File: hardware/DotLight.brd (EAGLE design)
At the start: 25.4 x 43.5 mm, 21 parts, among them Q1 BSH103, Q2 BSH103

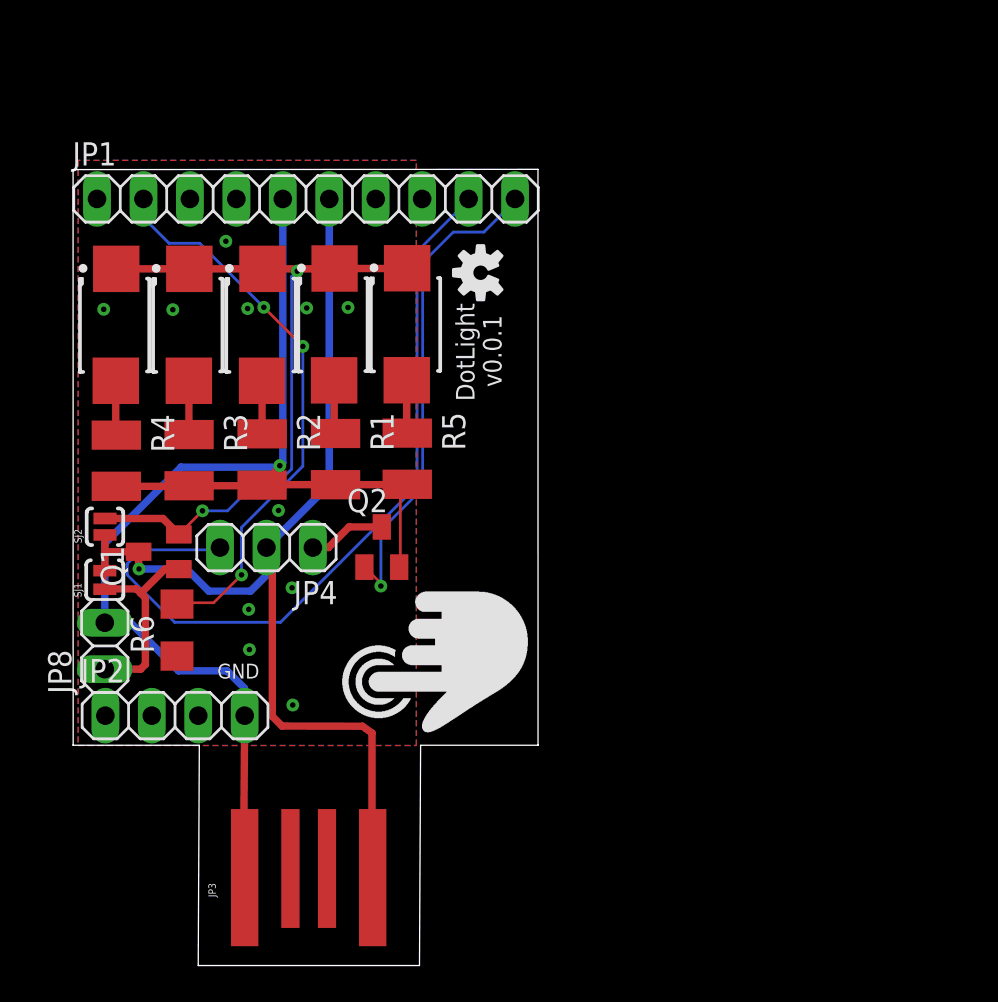
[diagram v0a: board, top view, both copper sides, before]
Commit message: Mirror parts for space for PIR
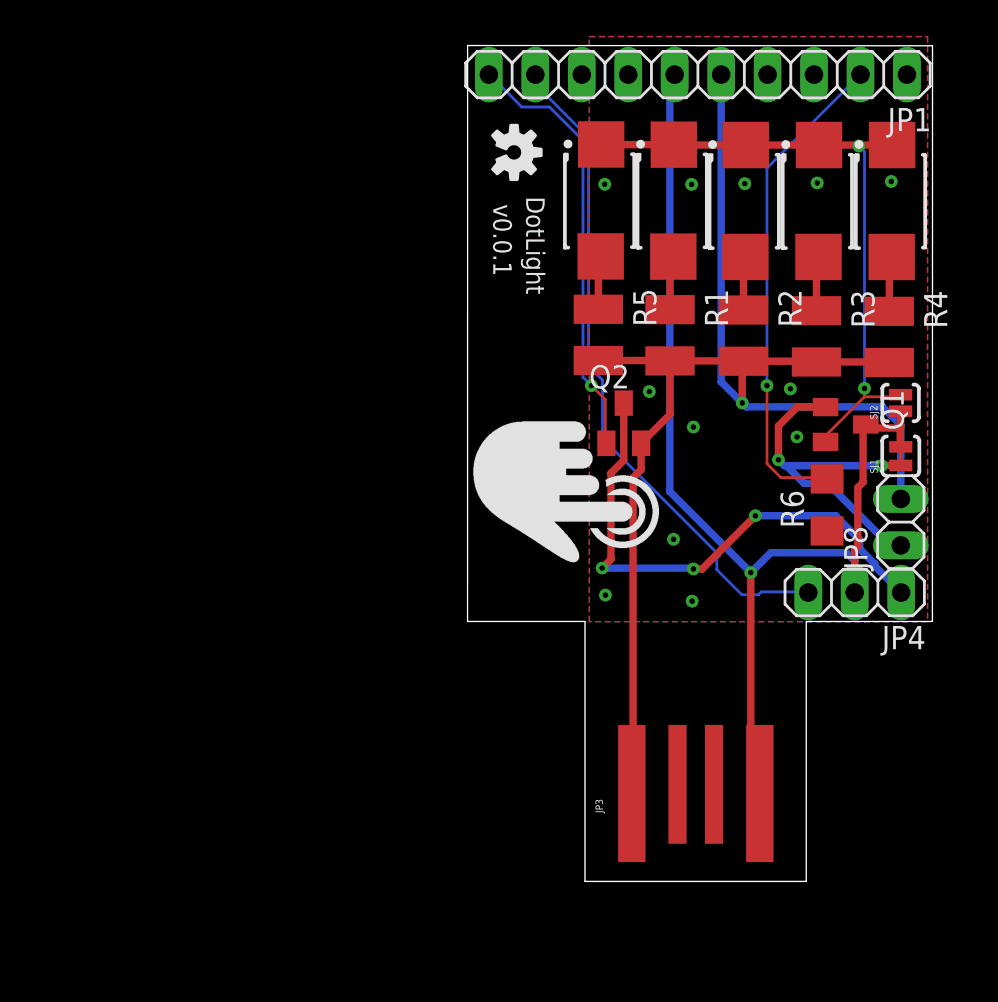
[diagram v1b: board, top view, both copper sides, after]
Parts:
- removed JP2: (no value), pinhead:1X04
- moved JP8 44.1 mm to (45.4, 23.3)
- moved SJ1 44.1 mm to (45.4, 26.9)
- moved SJ2 44.0 mm to (45.4, 29.8)
- moved LED3 43.0 mm to (44.9, 40.9)
- moved R4 42.8 mm to (44.8, 33.5)
- moved Q1 38.2 mm to (42.4, 28.7), turned to 270 degrees
- moved R6 36.2 mm to (41.4, 24.3)
- moved LED2 35.1 mm to (40.9, 40.9)
- moved R3 35.0 mm to (40.8, 33.5)
- moved JP4 32.3 mm to (42.9, 19.5)
- moved LED1 27.3 mm to (36.9, 40.9)
- moved R2 27.2 mm to (36.8, 33.5)
- moved JP1 22.5 mm to (34.3, 47.8), turned to 180 degrees
- moved JP3 21.7 mm to (34.2, 8.68)
- moved LED4 19.7 mm to (32.9, 40.9)
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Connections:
- removed net +3V3: JP2.3
- removed net SCL: JP2.2
- removed net SDA: JP2.1
- net GND: no longer JP2.4
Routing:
- net N$3: track 4.24 -> 29.2 mm, vias 0 -> 3
- net LEDS: track 11.0 -> 19.8 mm, vias 0 -> 2
- net MISO: track 42.9 -> 36.9 mm
- net VIN_PIN: track 57.7 -> 62.9 mm
- net N$4: track 40.3 -> 35.2 mm
- net ADC: track 30.7 -> 27.0 mm, vias 3 -> 1
- net MOSI: track 26.6 -> 23.7 mm
- net GND: track 72.1 -> 74.5 mm
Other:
- board size 25.4 x 43.5 mm -> 25.4 x 45.7 mm
- board text added: "LEDS ENABLE"
- board text added: "PIR"
- board text removed: "GND"

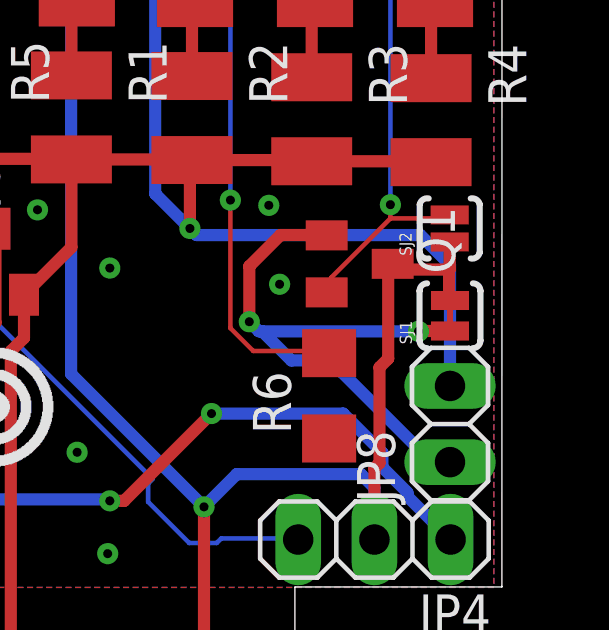
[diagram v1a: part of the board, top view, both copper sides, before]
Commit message: Mirror parts for space for PIR
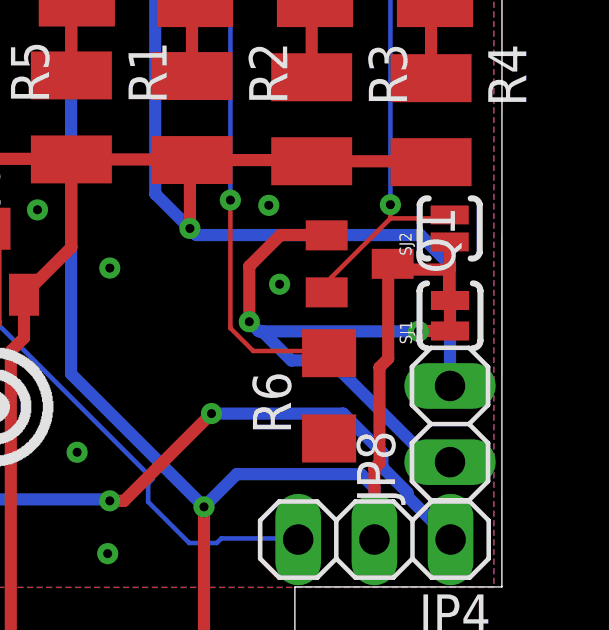
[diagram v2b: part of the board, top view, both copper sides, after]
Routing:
- net N$1: track 0.00 -> 0.73 mm
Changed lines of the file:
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@@
 <via x="43.1292" y="43.8912" extent="1-16" drill="0.3"/>
+</signal>
+<signal name="N$1">
+<wire x1="45.42" y1="27.32" x2="45.42" y2="26.59" width="0.4064" layer="1"/>
 </signal>
 </signals>

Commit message: Adjust solderjumpers
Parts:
- removed SJ1: SOLDERJUMPERTRACE, SparkFun-Retired:SJ_2S-TRACE
- moved JP1 21.2 mm to (13.4, 44.6)
- moved JP3 21.2 mm to (13.3, 5.47)
- moved JP8 21.2 mm to (24.5, 20.1)
- moved LED4 21.2 mm to (12.0, 37.7)
- moved LED5 21.2 mm to (8.04, 37.7)
- moved Q2 21.2 mm to (9.35, 25.5)
- moved R2 21.2 mm to (15.9, 30.3)
- moved R3 21.2 mm to (19.9, 30.3)
- moved R6 21.2 mm to (20.5, 21.1)
- moved JP4 21.2 mm to (22.0, 16.3)
- moved LED1 21.2 mm to (15.9, 37.7)
- moved LED2 21.2 mm to (19.9, 37.7)
- moved LED3 21.2 mm to (23.9, 37.7)
- moved LOGO1 21.2 mm to (3.35, 40.3)
- moved Q1 21.2 mm to (21.5, 25.4)
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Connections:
- net N$4 renamed GO
- net LEDS: no longer SJ1.1
- net VIN_PIN: no longer SJ1.2
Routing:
- net LEDS: track 19.8 -> 12.4 mm, vias 2 -> 1
- net GO: track 35.2 -> 42.6 mm
- net VIN_PIN: track 62.9 -> 61.8 mm
- net N$1: track 0.73 -> 0.00 mm
- net ADC: track 27.0 -> 27.6 mm
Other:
- board text added: "v0.1.0"
- board text removed: "v0.0.1"
